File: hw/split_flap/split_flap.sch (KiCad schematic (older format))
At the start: 4 parts, among them J17 EXPANDER_PORT, J19 POWER, U1 74HCT125, U2 NodeMCU_1.0_(ESP-12E)

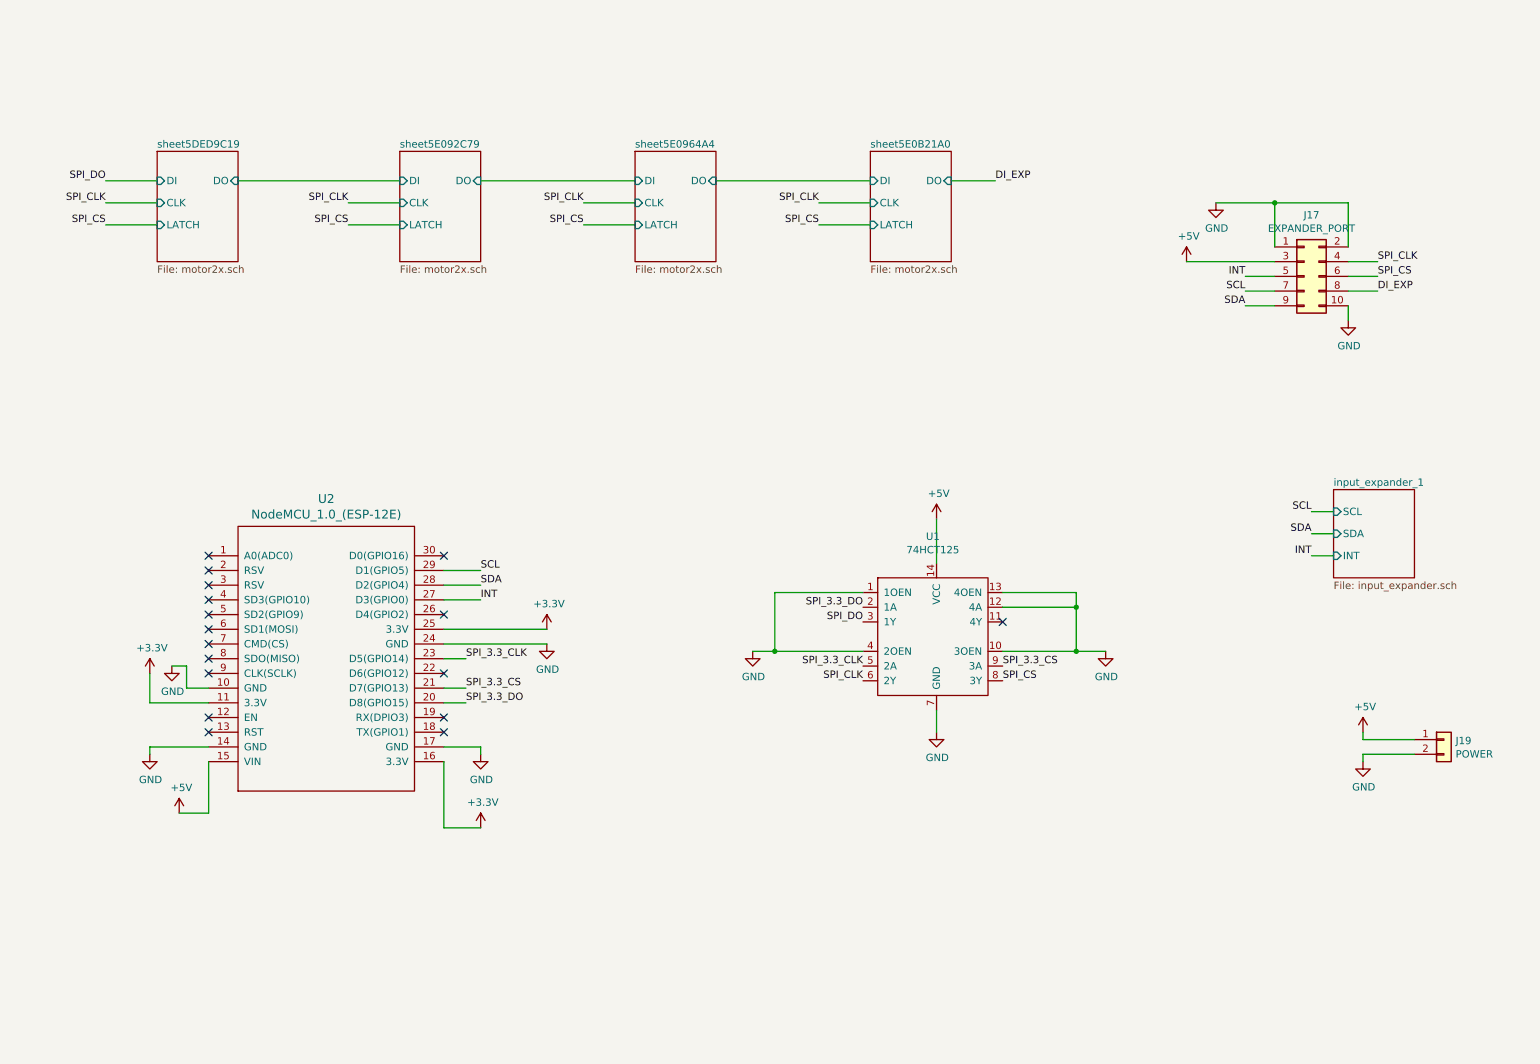
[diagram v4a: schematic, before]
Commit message: Rework PCB
Start routing all expanders
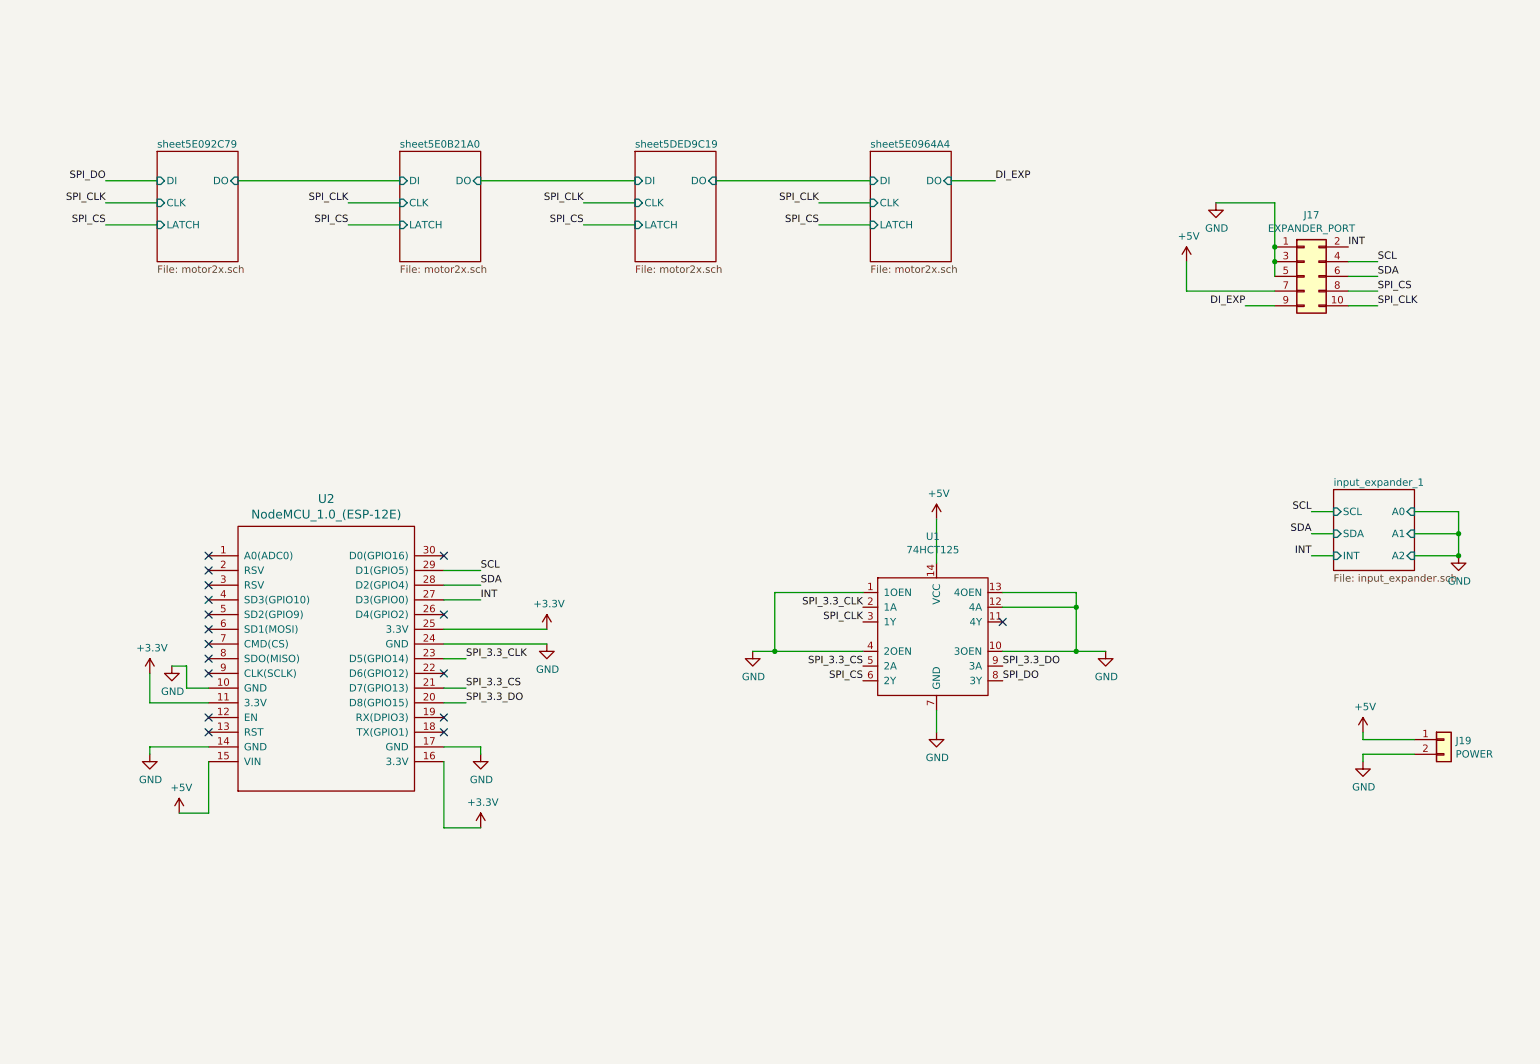
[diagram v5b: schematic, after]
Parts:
- U1: footprint (none) -> Package_SO:SOIC-14_3.9x8.7mm_P1.27mm
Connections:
- net +5V: now also J17.7 (Pin_7); no longer J17.3 (Pin_3)
- net DI_EXP: now also J17.9 (Pin_9); no longer J17.8 (Pin_8)
- net GND: now also J17.3 (Pin_3), J17.5 (Pin_5); no longer J17.10 (Pin_10), J17.2 (Pin_2)
- net INT: now also J17.2 (Pin_2); no longer J17.5 (Pin_5)
- net SCL: now also J17.4 (Pin_4); no longer J17.7 (Pin_7)
- net SDA: now also J17.6 (Pin_6); no longer J17.9 (Pin_9)
- net SPI_3.3_CLK: now also U1.2 (1A); no longer U1.5 (2A)
- net SPI_3.3_CS: now also U1.5 (2A); no longer U1.9 (3A)
- net SPI_3.3_DO: now also U1.9 (3A); no longer U1.2 (1A)
- net SPI_CLK: now also J17.10 (Pin_10), U1.3 (1Y); no longer J17.4 (Pin_4), U1.6 (2Y)
- net SPI_CS: now also J17.8 (Pin_8), U1.6 (2Y); no longer J17.6 (Pin_6), U1.8 (3Y)
- net SPI_DO: now also U1.8 (3Y); no longer U1.3 (1Y)
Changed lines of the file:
@@
 	1    0    0    -1
 $EndComp
-Text Label 8950 2550 2    50   ~ 0
+Text Label 9850 2350 0    50   ~ 0
 SCL
-Text Label 8950 2650 2    50   ~ 0
+Text Label 9850 2450 0    50   ~ 0
 SDA
 Wire Wire Line
-	8950 2550 9150 2550
-Wire Wire Line
 	9150 2650 8950 2650
 $Sheet
-S 1550 1600 550  750
+S 4800 1600 550  750
 U 5DED9C19
 F0 "sheet5DED9C19" 50
 F1 "motor2x.sch" 50
-F2 "DO" I R 2100 1800 50
-F3 "LATCH" I L 1550 2100 50
-F4 "DI" I L 1550 1800 50
-F5 "CLK" I L 1550 1950 50
+F2 "DO" I R 5350 1800 50
+F3 "LATCH" I L 4800 2100 50
+F4 "DI" I L 4800 1800 50
+F5 "CLK" I L 4800 1950 50
 $EndSheet
 NoConn ~ 1900 5550
@@
 $EndComp
 Wire Wire Line
-	9150 2350 8550 2350
-Wire Wire Line
 	9150 2250 9150 1950
 Wire Wire Line
 	9150 1950 8750 1950
-Wire Wire Line
-	9650 2250 9650 1950
-Wire Wire Line
-	9650 1950 9150 1950
-Connection ~ 9150 1950
 Wire Wire Line
 	3500 4850 4200 4850
@@
 Wire Wire Line
 	3500 4650 3750 4650
+Text Label 6350 4800 2    50   ~ 0
+SPI_CLK
+Wire Wire Line
+	1550 1800 1200 1800
+Text Label 7300 5200 0    50   ~ 0
+SPI_DO
+Wire Wire Line
+	1200 1950 1550 1950
 Text Label 6350 5200 2    50   ~ 0
-SPI_CLK
-Wire Wire Line
-	1550 1800 1200 1800
-Text Label 6350 4800 2    50   ~ 0
-SPI_DO
-Wire Wire Line
-	1200 1950 1550 1950
-Text Label 7300 5200 0    50   ~ 0
 SPI_CS
 Wire Wire Line
 	1200 2100 1550 2100
 $Sheet
-S 9550 3900 550  600
+S 9550 3900 550  550
 U 5E065378
 F0 "input_expander_1" 50
@@
 F3 "SDA" I L 9550 4200 50
 F4 "INT" I L 9550 4350 50
+F5 "A0" I R 10100 4050 50
+F6 "A1" I R 10100 4200 50
+F7 "A2" I R 10100 4350 50
 $EndSheet
 Text Label 2850 1950 2    50   ~ 0
@@
 	2850 2100 3200 2100
 $Sheet
-S 4800 1600 550  750
+S 6400 1600 550  750
 U 5E0964A4
 F0 "sheet5E0964A4" 50
 F1 "motor2x.sch" 50
-F2 "DO" I R 5350 1800 50
-F3 "LATCH" I L 4800 2100 50
-F4 "DI" I L 4800 1800 50
-F5 "CLK" I L 4800 1950 50
+F2 "DO" I R 6950 1800 50
+F3 "LATCH" I L 6400 2100 50
+F4 "DI" I L 6400 1800 50
+F5 "CLK" I L 6400 1950 50
 $EndSheet
 Text Label 4450 1950 2    50   ~ 0
@@
 Wire Wire Line
 	9400 4350 9550 4350
-Text Label 8950 2450 2    50   ~ 0
+Text Label 9650 2250 0    50   ~ 0
 INT
 Text Label 7250 1800 0    50   ~ 0
 DI_EXP
+Text Label 8950 2650 2    50   ~ 0
+DI_EXP
+Text Label 9850 2650 0    50   ~ 0
+SPI_CLK
 Text Label 9850 2550 0    50   ~ 0
-DI_EXP
-Wire Wire Line
-	9150 2450 8950 2450
-Text Label 9850 2350 0    50   ~ 0
-SPI_CLK
-Text Label 9850 2450 0    50   ~ 0
 SPI_CS
 Wire Wire Line
@@
 Wire Wire Line
 	9650 2550 9850 2550
-$Comp
-L power:GND #PWR07
-U 1 1 5E0D652A
-P 9650 2750
-F 0 "#PWR07" H 9650 2500 50  0001 C CNN
-F 1 "GND" H 9655 2577 50  0000 C CNN
-F 2 "" H 9650 2750 50  0001 C CNN
-F 3 "" H 9650 2750 50  0001 C CNN
-	1    9650 2750
-	1    0    0    -1
-$EndComp
-Wire Wire Line
-	9650 2650 9650 2750
 $Comp
 L 74HCT125:74HCT125 U1
@@
 F 0 "U1" H 6825 5581 50  0000 C CNN
 F 1 "74HCT125" H 6825 5490 50  0000 C CNN
-F 2 "" H 6850 4900 50  0001 C CNN
+F 2 "Package_SO:SOIC-14_3.9x8.7mm_P1.27mm" H 6850 4900 50  0001 C CNN
 F 3 "" H 6850 4900 50  0001 C CNN
 	1    6850 4900
@@
 Wire Wire Line
 	7300 5000 7800 5000
+Text Label 7300 5100 0    50   ~ 0
+SPI_3.3_DO
 Text Label 6350 4700 2    50   ~ 0
-SPI_3.3_DO
+SPI_3.3_CLK
 Text Label 6350 5100 2    50   ~ 0
-SPI_3.3_CLK
-Text Label 7300 5100 0    50   ~ 0
 SPI_3.3_CS
 $Sheet
-S 3200 1600 550  750
+S 1550 1600 550  750
 U 5E092C79
 F0 "sheet5E092C79" 50
+F1 "motor2x.sch" 50
+F2 "DO" I R 2100 1800 50
+F3 "LATCH" I L 1550 2100 50
+F4 "DI" I L 1550 1800 50
+F5 "CLK" I L 1550 1950 50
+$EndSheet
+$Sheet
+S 3200 1600 550  750
+U 5E0B21A0
+F0 "sheet5E0B21A0" 50
 F1 "motor2x.sch" 50
 F2 "DO" I R 3750 1800 50
@@
 F4 "DI" I L 3200 1800 50
 F5 "CLK" I L 3200 1950 50
-$EndSheet
-$Sheet
-S 6400 1600 550  750
-U 5E0B21A0
-F0 "sheet5E0B21A0" 50
-F1 "motor2x.sch" 50
-F2 "DO" I R 6950 1800 50
-F3 "LATCH" I L 6400 2100 50
-F4 "DI" I L 6400 1800 50
-F5 "CLK" I L 6400 1950 50
 $EndSheet
 Wire Wire Line
@@
 Text Label 1200 1800 2    50   ~ 0
 SPI_DO
+$Comp
+L power:GND #PWR014
+U 1 1 5DF4FEB1
+P 10400 4350
+F 0 "#PWR014" H 10400 4100 50  0001 C CNN
+F 1 "GND" H 10405 4177 50  0000 C CNN
+F 2 "" H 10400 4350 50  0001 C CNN
+F 3 "" H 10400 4350 50  0001 C CNN
+	1    10400 4350
+	1    0    0    -1
+$EndComp
+Wire Wire Line
+	10100 4050 10400 4050
+Wire Wire Line
+	10400 4050 10400 4200
+Wire Wire Line
+	10100 4200 10400 4200
+Connection ~ 10400 4200
+Wire Wire Line
+	10400 4200 10400 4350
+Wire Wire Line
+	10100 4350 10400 4350
+Connection ~ 10400 4350
+Wire Wire Line
+	9650 2650 9850 2650
+Wire Wire Line
+	9150 2550 8550 2550
+Wire Wire Line
+	8550 2550 8550 2350
+Wire Wire Line
+	9150 2450 9150 2350
+Wire Wire Line
+	9150 2350 9150 2250
+Connection ~ 9150 2350
+Connection ~ 9150 2250
 $EndSCHEMATC

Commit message: Route new PCB completely.
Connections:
- net SPI_3.3_CS: now also U2.20 (D8(GPIO15)); no longer U2.21 (D7(GPIO13))
- net SPI_3.3_DO: now also U2.21 (D7(GPIO13)); no longer U2.20 (D8(GPIO15))
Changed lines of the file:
@@
 SPI_3.3_CLK
 Text Label 3650 5350 0    50   ~ 0
-SPI_3.3_DO
-Text Label 3650 5250 0    50   ~ 0
 SPI_3.3_CS
 Wire Wire Line
@@
 Connection ~ 9150 2350
 Connection ~ 9150 2250
+Text Label 3650 5250 0    50   ~ 0
+SPI_3.3_DO
 $EndSCHEMATC

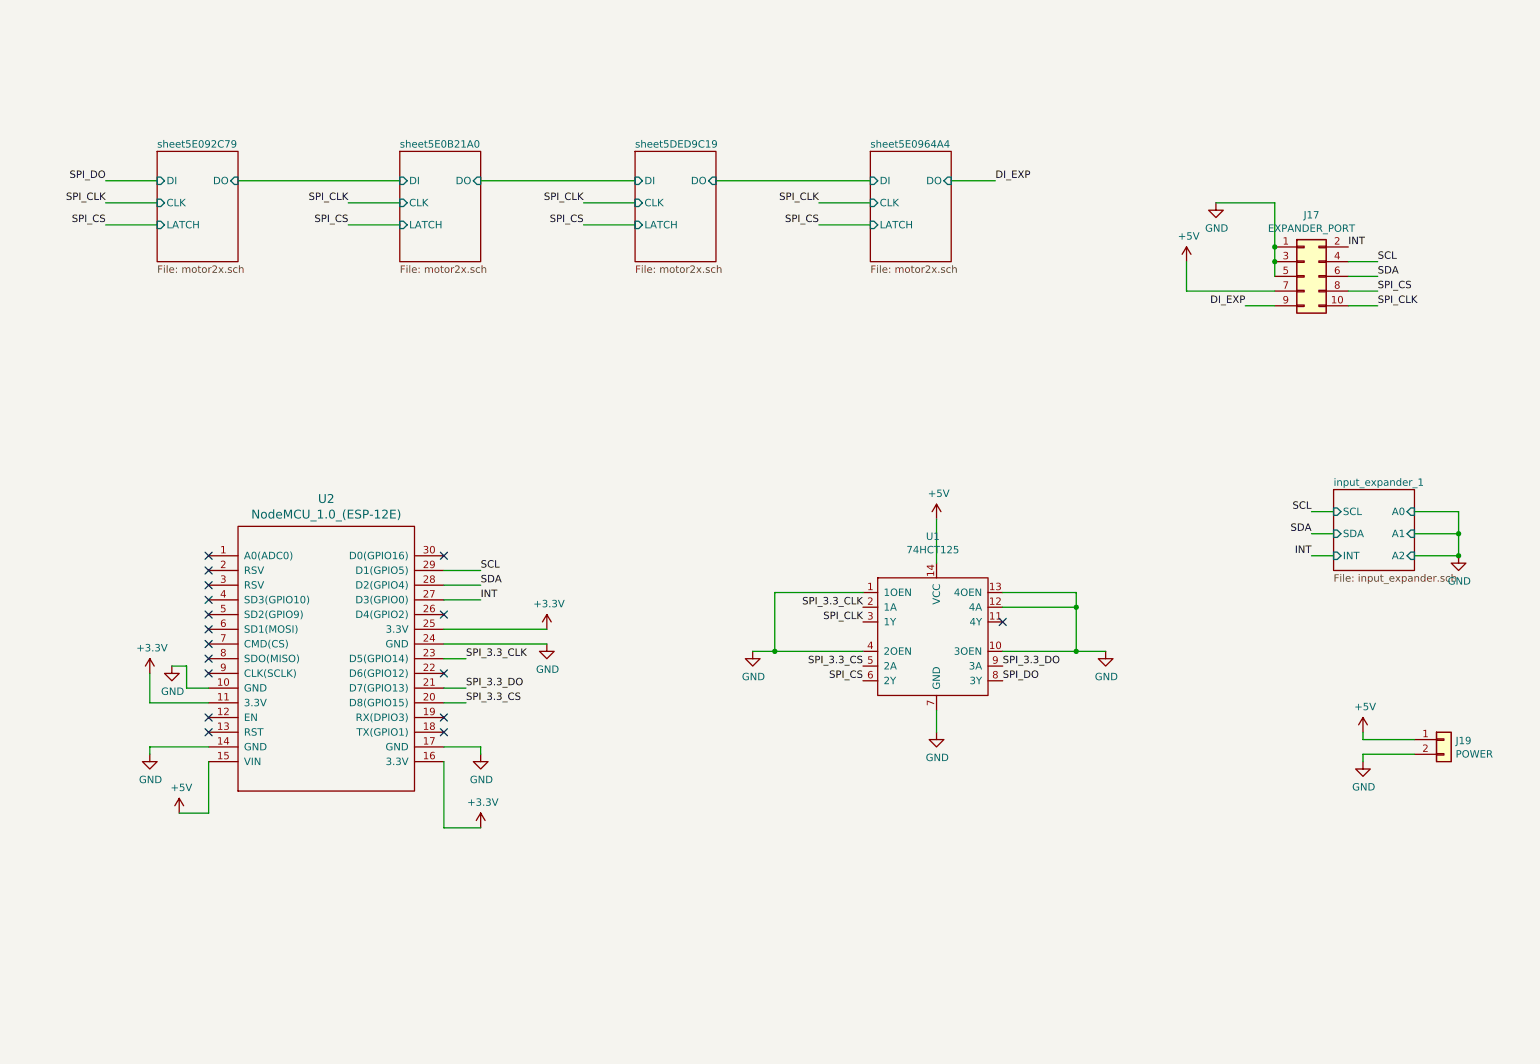
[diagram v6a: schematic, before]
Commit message: Add VCC for motors
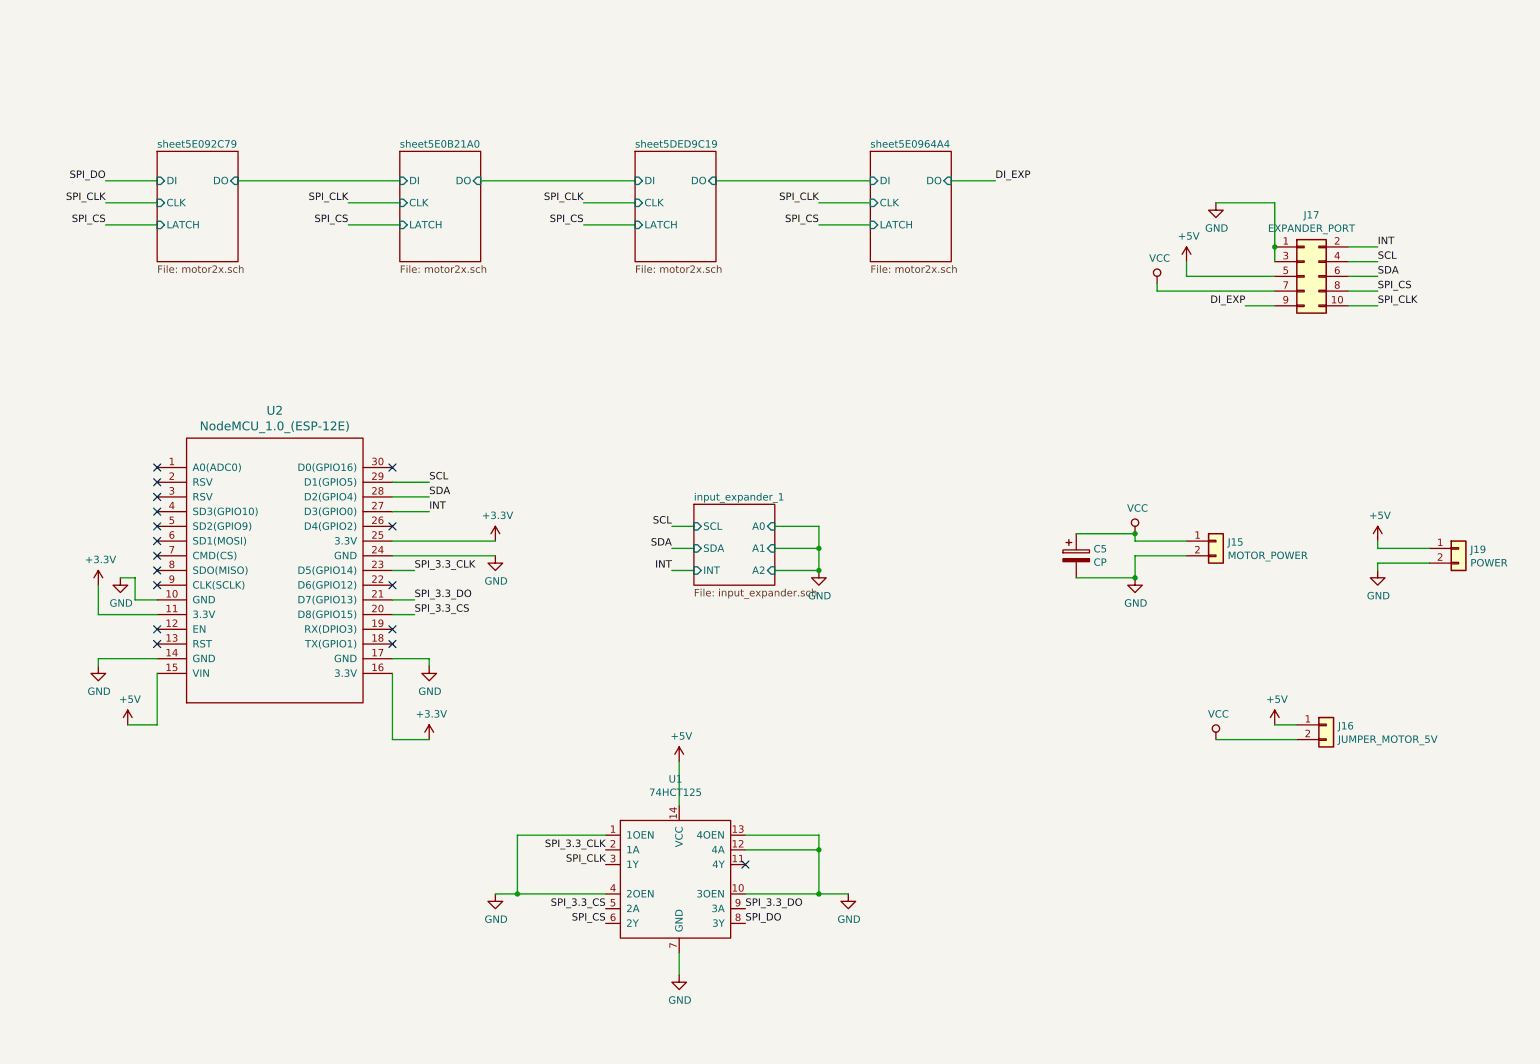
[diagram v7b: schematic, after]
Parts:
- added C5: CP, Capacitor_THT:CP_Radial_D6.3mm_P2.50mm, symbol Device:CP
- added J15: MOTOR_POWER, Connector_JST:JST_XH_B2B-XH-A_1x02_P2.50mm_Vertical, symbol Connector_Generic:Conn_01x02
- added J16: JUMPER_MOTOR_5V, Connector_PinHeader_2.54mm:PinHeader_1x02_P2.54mm_Vertical, symbol Connector_Generic:Conn_01x02
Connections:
- net +5V: now also J17.5 (Pin_5), J16.1 (Pin_1); no longer J17.7 (Pin_7)
- net GND: now also C5.2, J15.2 (Pin_2); no longer J17.5 (Pin_5)
- new net VCC: C5.1, J15.1 (Pin_1), J16.2 (Pin_2), J17.7 (Pin_7)
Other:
- moved on the sheet: J19, U1, U2
